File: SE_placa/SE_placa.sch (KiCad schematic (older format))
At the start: 49 parts, among them J1 5V, J2 Micro_SD_Card_Det_Hirose_DM3AT, J3 Conn_02x07_ESP32_IO, J4 I2C-0, J5 I2C-1, J6 Conn_02x03_LORA_IO, J7 U.FL-R-SMT(01), J8 UART, J9 Connector Bateria, Q1 BSS138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

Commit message: Actualizacion PCB
Organizo archivos, agrego nuevos elementos a footprint, actualizo net list y actualizo PCB, agrego modelos 3D disponibles. Listo para iniciar ruteo
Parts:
- J7: symbol U.FL-R-SMT_01_:U.FL-R-SMT(01) -> SE_placa-rescue:U.FL-R-SMT(01)-U.FL-R-SMT_01_
- SW1, SW2: footprint B3U-1000P:SW_B3U-1000P -> Button_Switch_SMD:SW_SPST_CK_RS282G05A3
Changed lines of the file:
@@
 F 0 "SW1" H 2675 7035 50  0000 C CNN
 F 1 "SW_Push_Download" H 2675 6944 50  0000 C CNN
-F 2 "B3U-1000P:SW_B3U-1000P" H 2675 6950 50  0001 C CNN
+F 2 "Button_Switch_SMD:SW_SPST_CK_RS282G05A3" H 2675 6950 50  0001 C CNN
 F 3 "~" H 2675 6950 50  0001 C CNN
 	1    2675 6750
@@
 F 0 "SW2" H 2990 4680 50  0000 C CNN
 F 1 "SW_Push_ESP_RST" H 3255 4595 50  0000 C CNN
-F 2 "B3U-1000P:SW_B3U-1000P" H 3275 4625 50  0001 C CNN
+F 2 "Button_Switch_SMD:SW_SPST_CK_RS282G05A3" H 3275 4625 50  0001 C CNN
 F 3 "~" H 3275 4625 50  0001 C CNN
 	1    3275 4425
@@
 $EndComp
 $Comp
-L U.FL-R-SMT_01_:U.FL-R-SMT(01) J7
+L SE_placa-rescue:U.FL-R-SMT(01)-U.FL-R-SMT_01_ J7
 U 1 1 6198A7A3
 P 14750 2600

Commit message: Organizar integrado rev A
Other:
- note added: "I2C-Segundo sensor\n"
- note added: "Indicador VCC Lora"
- note added: "Indicador VCC general\n"
- note removed: "I2C-spare"
- moved on the sheet: J4, J5, R12, R13
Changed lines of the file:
@@
 Sheet 1 2
 Title "SE_1"
-Date "2021-05-05"
-Rev "1.0"
+Date "2021-07-01"
+Rev "B"
 Comp "Universidad Nacional de Colombia"
 Comment1 "Wilson Poveda"
@@
 L Connector_Generic:Conn_01x04 J4
 U 1 1 60980048
-P 9375 8550
-F 0 "J4" H 9455 8542 50  0000 L CNN
-F 1 "I2C-0" H 9455 8451 50  0000 L CNN
-F 2 "Connector_PinSocket_2.54mm:PinSocket_1x04_P2.54mm_Vertical" H 9375 8550 50  0001 C CNN
-F 3 "~" H 9375 8550 50  0001 C CNN
-	1    9375 8550
+P 9625 8775
+F 0 "J4" H 9705 8767 50  0000 L CNN
+F 1 "I2C-0" H 9705 8676 50  0000 L CNN
+F 2 "Connector_PinSocket_2.54mm:PinSocket_1x04_P2.54mm_Vertical" H 9625 8775 50  0001 C CNN
+F 3 "~" H 9625 8775 50  0001 C CNN
+	1    9625 8775
 	1    0    0    -1
 $EndComp
@@
 Text Label 11100 3000 0    50   ~ 0
 I2C-SDA
-Text Label 8600 8450 0    50   ~ 0
+Text Label 8850 8675 0    50   ~ 0
 I2C-SDA
-Text Label 8600 8550 0    50   ~ 0
+Text Label 8850 8775 0    50   ~ 0
 I2C-SCL
 Text Notes 750  910  0    157  ~ 31
 POWER
-Text Notes 8550 9450 0    118  ~ 0
+Text Notes 8250 8300 0    118  ~ 0
 I2C- BMP180 - BY-68
 Text Notes 715  8240 0    157  ~ 31
@@
 L power:GND #PWR018
 U 1 1 6177D577
-P 8225 8750
-F 0 "#PWR018" H 8225 8500 50  0001 C CNN
-F 1 "GND" H 8230 8577 50  0000 C CNN
-F 2 "" H 8225 8750 50  0001 C CNN
-F 3 "" H 8225 8750 50  0001 C CNN
-	1    8225 8750
+P 8475 8975
+F 0 "#PWR018" H 8475 8725 50  0001 C CNN
+F 1 "GND" H 8480 8802 50  0000 C CNN
+F 2 "" H 8475 8975 50  0001 C CNN
+F 3 "" H 8475 8975 50  0001 C CNN
+	1    8475 8975
 	1    0    0    -1
 $EndComp
@@
 Text Notes 7380 8310 0    157  ~ 31
 I2C\n
-Text Notes 8750 10950 0    118  ~ 0
-I2C-spare
+Text Notes 8600 9900 0    118  ~ 0
+I2C-Segundo sensor\n
 $Comp
 L Connector_Generic:Conn_02x03_Top_Bottom J6
@@
 L Device:R R13
 U 1 1 60AD4FD0
-P 8025 10500
-F 0 "R13" V 7925 10500 50  0000 C CNN
-F 1 "4.7K(5%)" V 8125 10525 50  0000 C CNN
-F 2 "Resistor_SMD:R_0805_2012Metric_Pad1.20x1.40mm_HandSolder" V 7955 10500 50  0001 C CNN
-F 3 "~" H 8025 10500 50  0001 C CNN
-	1    8025 10500
+P 8075 10775
+F 0 "R13" V 7975 10775 50  0000 C CNN
+F 1 "4.7K(5%)" V 8175 10800 50  0000 C CNN
+F 2 "Resistor_SMD:R_0805_2012Metric_Pad1.20x1.40mm_HandSolder" V 8005 10775 50  0001 C CNN
+F 3 "~" H 8075 10775 50  0001 C CNN
+	1    8075 10775
 	0    1    1    0
 $EndComp
@@
 L Device:R R12
 U 1 1 60AD5CFB
-P 8025 9900
-F 0 "R12" V 7818 9900 50  0000 C CNN
-F 1 "4.7K(5%)" V 7909 9900 50  0000 C CNN
-F 2 "Resistor_SMD:R_0805_2012Metric_Pad1.20x1.40mm_HandSolder" V 7955 9900 50  0001 C CNN
-F 3 "~" H 8025 9900 50  0001 C CNN
-	1    8025 9900
+P 8075 10175
+F 0 "R12" V 7868 10175 50  0000 C CNN
+F 1 "4.7K(5%)" V 7959 10175 50  0000 C CNN
+F 2 "Resistor_SMD:R_0805_2012Metric_Pad1.20x1.40mm_HandSolder" V 8005 10175 50  0001 C CNN
+F 3 "~" H 8075 10175 50  0001 C CNN
+	1    8075 10175
 	0    1    1    0
 $EndComp
 Wire Wire Line
-	7875 10500 7875 10200
-Wire Wire Line
-	7875 10200 7575 10200
-Connection ~ 7875 10200
-Wire Wire Line
-	7875 10200 7875 9900
+	7925 10775 7925 10475
+Wire Wire Line
+	7925 10475 7625 10475
+Connection ~ 7925 10475
+Wire Wire Line
+	7925 10475 7925 10175
 Wire Wire Line
 	9300 2400 9000 2400
@@
 Connection ~ 13950 6550
 Wire Wire Line
-	8600 8450 9175 8450
-Wire Wire Line
-	8600 8550 9175 8550
+	8850 8675 9425 8675
+Wire Wire Line
+	8850 8775 9425 8775
 $Comp
 L power:+3V3 #PWR019
 U 1 1 61EE58C6
-P 8550 8825
-F 0 "#PWR019" H 8550 8675 50  0001 C CNN
-F 1 "+3V3" H 8565 8998 50  0000 C CNN
-F 2 "" H 8550 8825 50  0001 C CNN
-F 3 "" H 8550 8825 50  0001 C CNN
-	1    8550 8825
+P 8800 9050
+F 0 "#PWR019" H 8800 8900 50  0001 C CNN
+F 1 "+3V3" H 8815 9223 50  0000 C CNN
+F 2 "" H 8800 9050 50  0001 C CNN
+F 3 "" H 8800 9050 50  0001 C CNN
+	1    8800 9050
 	-1   0    0    1
 $EndComp
 Wire Wire Line
-	8225 8650 8225 8750
-Wire Wire Line
-	8225 8650 9175 8650
-Wire Wire Line
-	8550 8750 8550 8825
-Wire Wire Line
-	8550 8750 9175 8750
+	8475 8875 8475 8975
+Wire Wire Line
+	8475 8875 9425 8875
+Wire Wire Line
+	8800 8975 8800 9050
+Wire Wire Line
+	8800 8975 9425 8975
 $Comp
 L power:+3V3 #PWR013
 U 1 1 61F0C445
-P 7575 10200
-F 0 "#PWR013" H 7575 10050 50  0001 C CNN
-F 1 "+3V3" H 7590 10373 50  0000 C CNN
-F 2 "" H 7575 10200 50  0001 C CNN
-F 3 "" H 7575 10200 50  0001 C CNN
-	1    7575 10200
-	1    0    0    -1
-$EndComp
-Wire Wire Line
-	8175 9900 8550 9900
-Wire Wire Line
-	8175 10500 8575 10500
-Text Label 8550 9900 0    50   ~ 0
+P 7625 10475
+F 0 "#PWR013" H 7625 10325 50  0001 C CNN
+F 1 "+3V3" H 7640 10648 50  0000 C CNN
+F 2 "" H 7625 10475 50  0001 C CNN
+F 3 "" H 7625 10475 50  0001 C CNN
+	1    7625 10475
+	1    0    0    -1
+$EndComp
+Wire Wire Line
+	8225 10175 8600 10175
+Wire Wire Line
+	8225 10775 8625 10775
+Text Label 8600 10175 0    50   ~ 0
 I2C-SDA
-Text Label 8575 10500 0    50   ~ 0
+Text Label 8625 10775 0    50   ~ 0
 I2C-SCL
 $Comp
 L Connector_Generic:Conn_01x04 J5
 U 1 1 61FC148A
-P 10800 9975
-F 0 "J5" H 10880 9967 50  0000 L CNN
-F 1 "I2C-1" H 10880 9876 50  0000 L CNN
-F 2 "Connector_PinSocket_2.54mm:PinSocket_1x04_P2.54mm_Vertical" H 10800 9975 50  0001 C CNN
-F 3 "~" H 10800 9975 50  0001 C CNN
-	1    10800 9975
-	1    0    0    -1
-$EndComp
-Text Label 10025 9875 0    50   ~ 0
+P 10850 10250
+F 0 "J5" H 10930 10242 50  0000 L CNN
+F 1 "I2C-1" H 10930 10151 50  0000 L CNN
+F 2 "Connector_PinSocket_2.54mm:PinSocket_1x04_P2.54mm_Vertical" H 10850 10250 50  0001 C CNN
+F 3 "~" H 10850 10250 50  0001 C CNN
+	1    10850 10250
+	1    0    0    -1
+$EndComp
+Text Label 10075 10150 0    50   ~ 0
 I2C-SDA
-Text Label 10025 9975 0    50   ~ 0
+Text Label 10075 10250 0    50   ~ 0
 I2C-SCL
 $Comp
 L power:GND #PWR022
 U 1 1 61FC16B4
-P 9650 10175
-F 0 "#PWR022" H 9650 9925 50  0001 C CNN
-F 1 "GND" H 9655 10002 50  0000 C CNN
-F 2 "" H 9650 10175 50  0001 C CNN
-F 3 "" H 9650 10175 50  0001 C CNN
-	1    9650 10175
-	1    0    0    -1
-$EndComp
-Wire Wire Line
-	10025 9875 10600 9875
-Wire Wire Line
-	10025 9975 10600 9975
+P 9700 10450
+F 0 "#PWR022" H 9700 10200 50  0001 C CNN
+F 1 "GND" H 9705 10277 50  0000 C CNN
+F 2 "" H 9700 10450 50  0001 C CNN
+F 3 "" H 9700 10450 50  0001 C CNN
+	1    9700 10450
+	1    0    0    -1
+$EndComp
+Wire Wire Line
+	10075 10150 10650 10150
+Wire Wire Line
+	10075 10250 10650 10250
 $Comp
 L power:+3V3 #PWR023
 U 1 1 61FC16C0
-P 9975 10250
-F 0 "#PWR023" H 9975 10100 50  0001 C CNN
-F 1 "+3V3" H 9990 10423 50  0000 C CNN
-F 2 "" H 9975 10250 50  0001 C CNN
-F 3 "" H 9975 10250 50  0001 C CNN
-	1    9975 10250
+P 10025 10525
+F 0 "#PWR023" H 10025 10375 50  0001 C CNN
+F 1 "+3V3" H 10040 10698 50  0000 C CNN
+F 2 "" H 10025 10525 50  0001 C CNN
+F 3 "" H 10025 10525 50  0001 C CNN
+	1    10025 10525
 	-1   0    0    1
 $EndComp
 Wire Wire Line
-	9650 10075 9650 10175
-Wire Wire Line
-	9650 10075 10600 10075
-Wire Wire Line
-	9975 10175 9975 10250
-Wire Wire Line
-	9975 10175 10600 10175
+	9700 10350 9700 10450
+Wire Wire Line
+	9700 10350 10650 10350
+Wire Wire Line
+	10025 10450 10025 10525
+Wire Wire Line
+	10025 10450 10650 10450
 $Comp
 L power:+3V3 #PWR026
@@
 Wire Wire Line
 	15325 9475 15325 9575
+Text Notes 12125 8900 0    50   ~ 0
+Indicador VCC general\n
+Text Notes 14025 9725 0    50   ~ 0
+Indicador VCC Lora
 $EndSCHEMATC

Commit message: Ubicaciones de librerias de absolutas a relativas
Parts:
- J7: footprint U:HRS_U.FL-R-SMT(01) -> HRS_U.FL-R-SMT(01)
- U1: symbol esp32-wrover:ESP32-WROVER -> SE_placa-rescue:ESP32-WROVER-esp32-wrover
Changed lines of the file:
@@
 F 0 "J7" H 14952 2640 50  0000 L CNN
 F 1 "U.FL-R-SMT(01)" H 14995 2525 50  0000 L CNN
-F 2 "U:HRS_U.FL-R-SMT(01)" H 14750 2600 50  0001 L BNN
+F 2 "HRS_U.FL-R-SMT(01)" H 14750 2600 50  0001 L BNN
 F 3 "https://www.sigmaelectronica.net/producto/con-u-fl-smd-m/" H 14750 2600 50  0001 L BNN
 F 4 "Hirose" H 14750 2600 50  0001 L BNN "MF"
@@
 	9300 3900 8800 3900
 $Comp
-L esp32-wrover:ESP32-WROVER U1
+L SE_placa-rescue:ESP32-WROVER-esp32-wrover U1
 U 1 1 6077AD20
 P 10200 3150
@@
 F 1 "Micro_SD_Card_Det_Hirose_DM3AT" H 5100 10526 50  0000 C CNN
 F 2 "Connector_Card:microSD_HC_Hirose_DM3AT-SF-PEJM5" H 7200 10500 50  0001 C CNN
-F 3 "https://www.sigmaelectronica.net/producto/dm3at/" H 5150 9900 50  0001 C CNN
+F 3 "https://www.hirose.com/product/en/download_file/key_name/DM3/category/Catalog/doc_file_id/49662/?file_category_id=4&item_id=195&is_series=1" H 5150 9900 50  0001 C CNN
 	1    5150 9800
 	1    0    0    -1

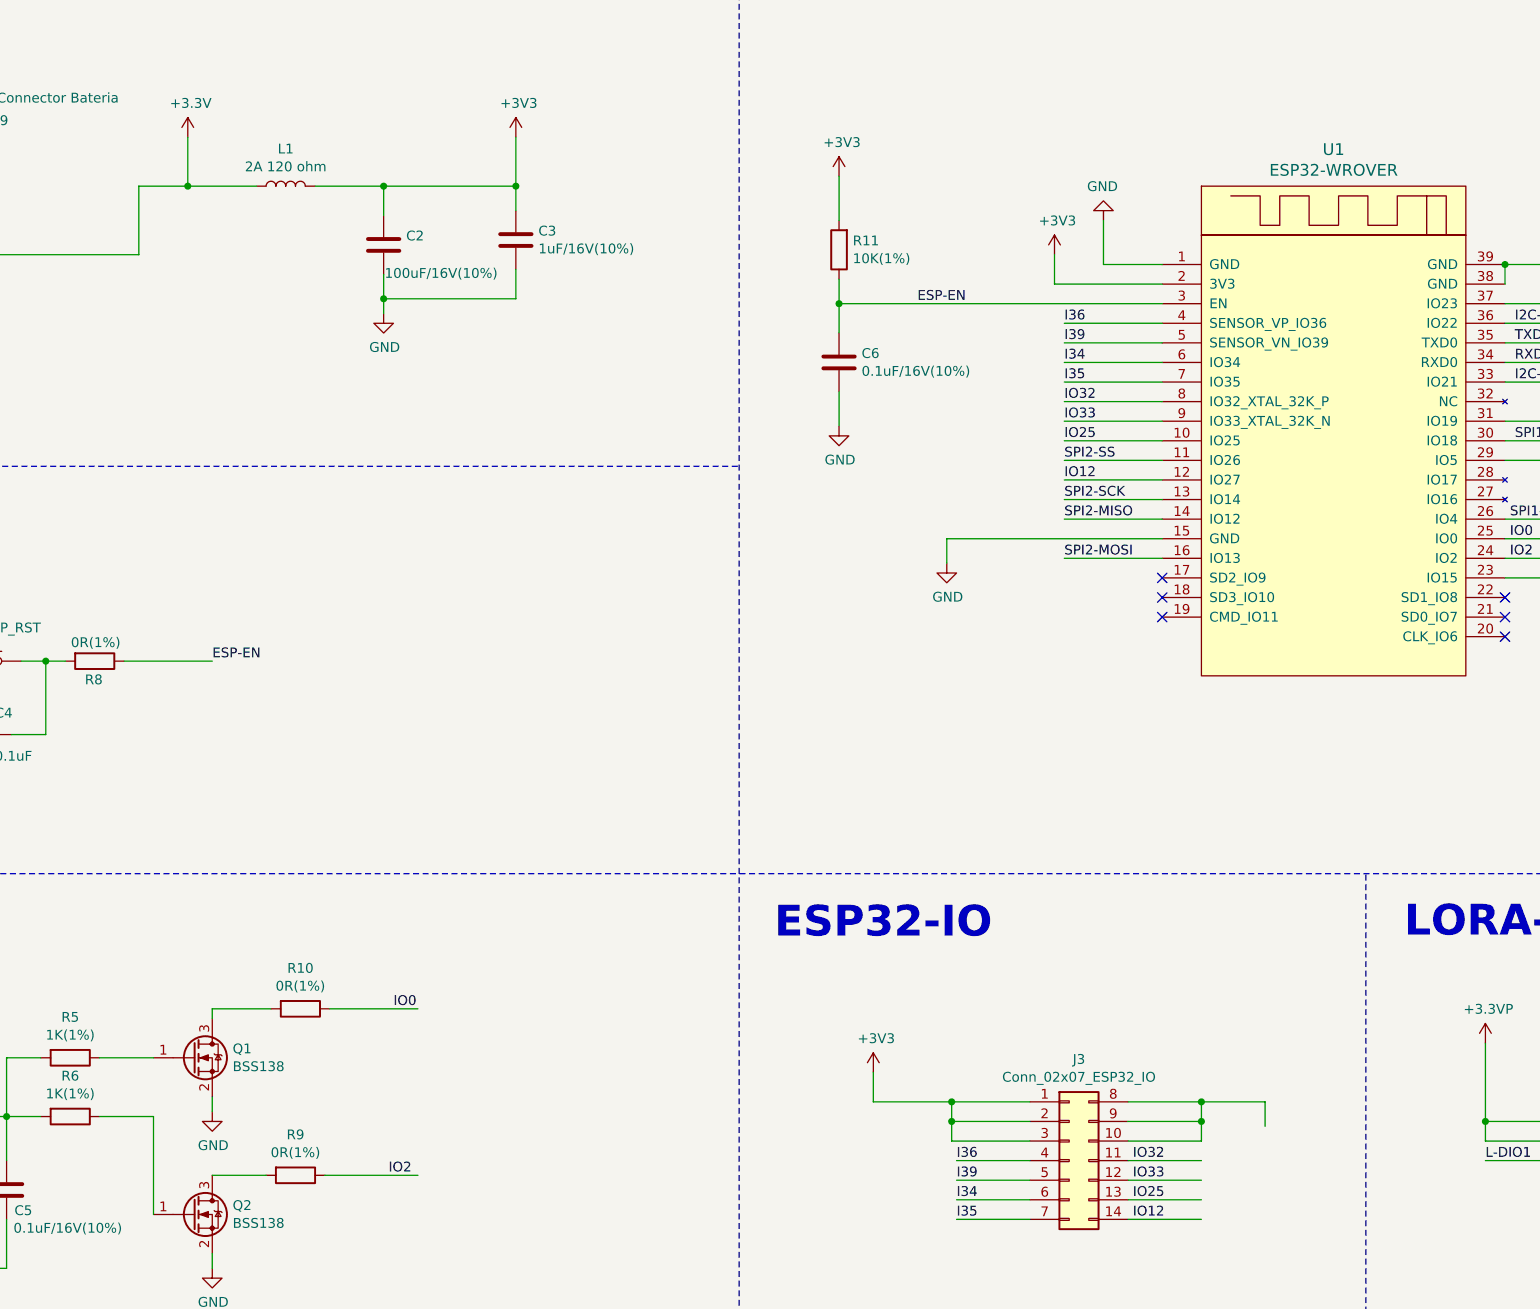
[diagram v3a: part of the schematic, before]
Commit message: ruteo 1
1. Agregados mounting holes 2.5 mm
2. Reordeno elementos para hacer mas facil el ruteo.
3. Ordeno los leds para indicar mejor el estado de lora y alimentacion general
4. Ordeno lesd y conectores de bateria y alimentacion por panel
giro conectores de I/o de lora
en general se dejaron por grupos los elementos de acuerdo al tipo de funcion dentro de la placa
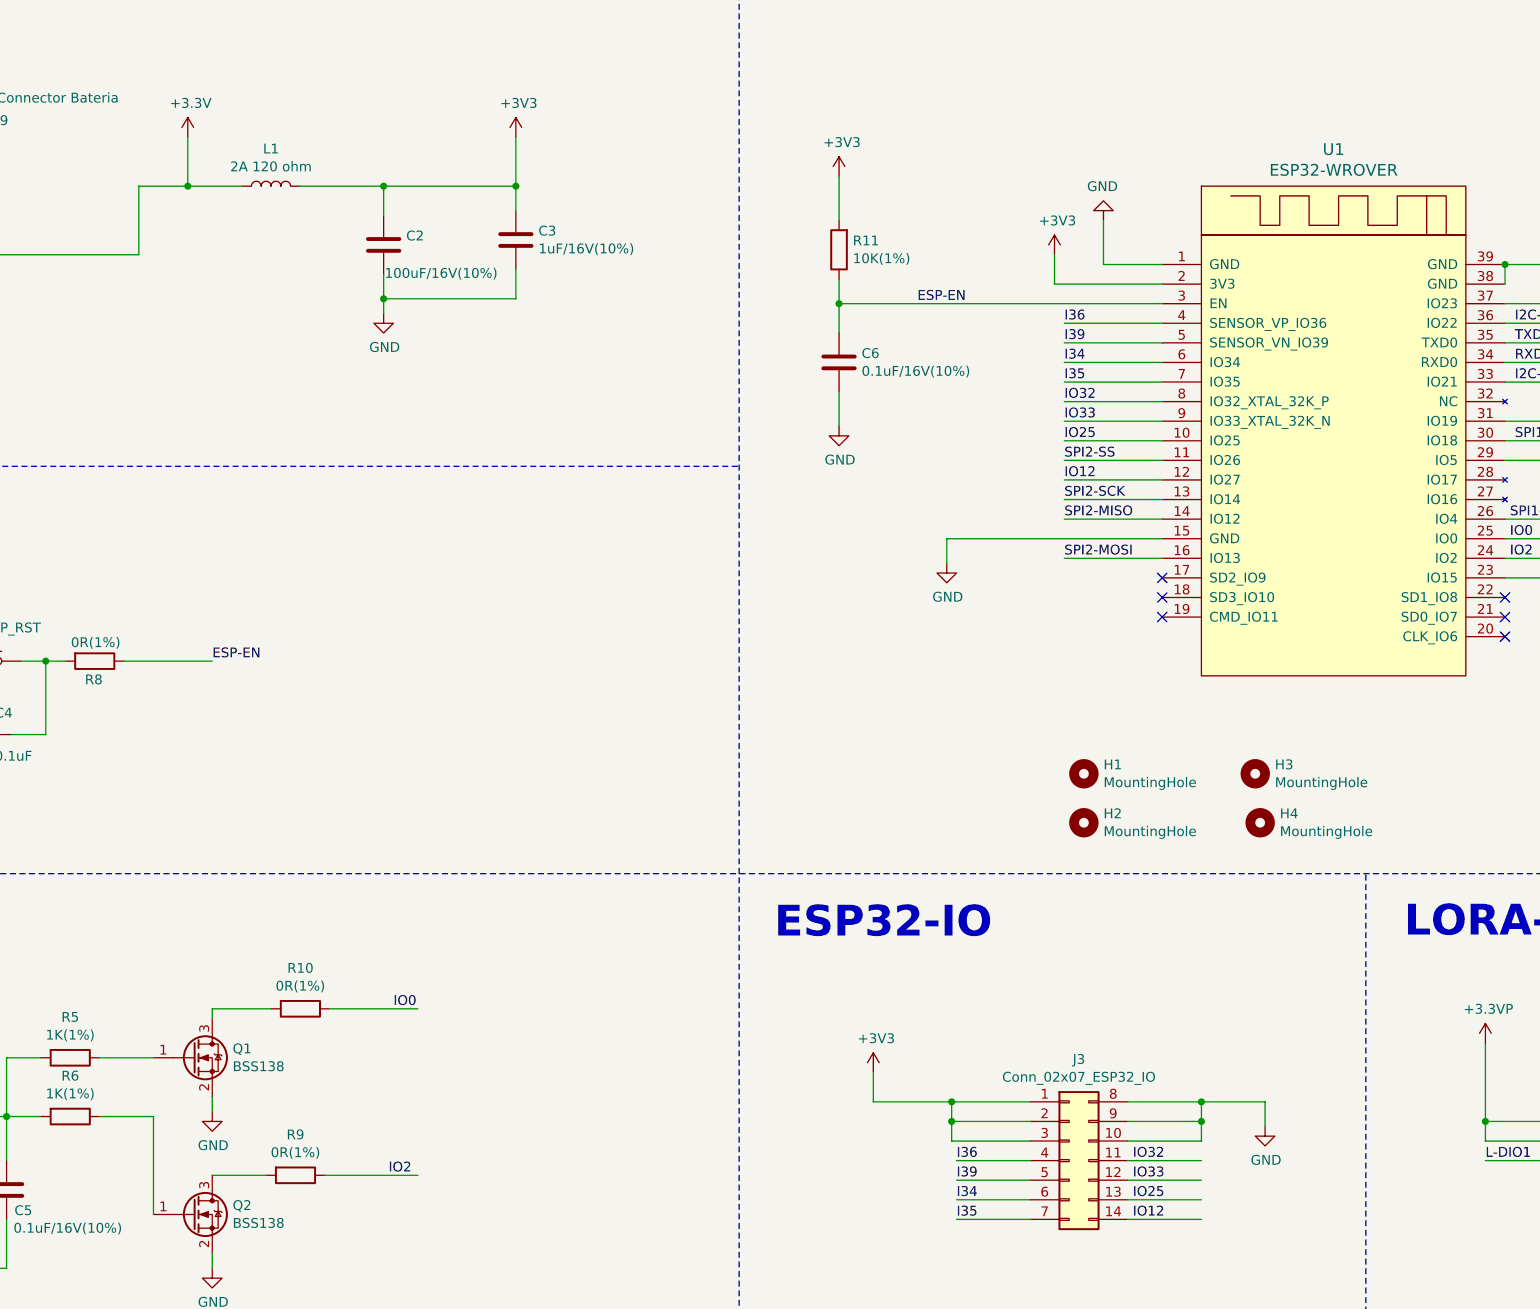
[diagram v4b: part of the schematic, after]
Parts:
- added H1, H2, H3, H4: MountingHole, MountingHole:MountingHole_2.5mm_Pad, symbol Mechanical:MountingHole
- J7: footprint HRS_U.FL-R-SMT(01) -> U:HRS_U.FL-R-SMT(01)
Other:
- moved on the sheet: L1
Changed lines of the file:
@@
 F 0 "J7" H 14952 2640 50  0000 L CNN
 F 1 "U.FL-R-SMT(01)" H 14995 2525 50  0000 L CNN
-F 2 "HRS_U.FL-R-SMT(01)" H 14750 2600 50  0001 L BNN
+F 2 "U:HRS_U.FL-R-SMT(01)" H 14750 2600 50  0001 L BNN
 F 3 "https://www.sigmaelectronica.net/producto/con-u-fl-smd-m/" H 14750 2600 50  0001 L BNN
 F 4 "Hirose" H 14750 2600 50  0001 L BNN "MF"
@@
 	5325 2450 5325 2575
 Wire Wire Line
-	5325 2000 6000 2000
-Wire Wire Line
 	5325 2150 5325 2000
 Wire Wire Line
@@
 Wire Wire Line
 	6000 2000 6000 1750
-Connection ~ 5325 2000
-Wire Wire Line
-	4975 2000 5325 2000
-Wire Wire Line
-	4325 2000 4675 2000
-Wire Wire Line
-	4325 1750 4325 2000
-Connection ~ 4325 2000
 $Comp
 L power:+3V3 #PWR043
@@
 L Device:L L1
 U 1 1 60B718E1
-P 4825 2000
+P 4750 2000
 AR Path="/60B718E1" Ref="L1"  Part="1"
 AR Path="/609FB393/60B718E1" Ref="L?"  Part="1"
-F 0 "L1" V 5015 2000 50  0000 C CNN
-F 1 "2A 120 ohm" V 4924 2000 50  0000 C CNN
-F 2 "Inductor_SMD:L_0805_2012Metric_Pad1.15x1.40mm_HandSolder" H 4825 2000 50  0001 C CNN
-F 3 "~" H 4825 2000 50  0001 C CNN
-	1    4825 2000
+F 0 "L1" V 4940 2000 50  0000 C CNN
+F 1 "2A 120 ohm" V 4849 2000 50  0000 C CNN
+F 2 "Inductor_SMD:L_0805_2012Metric_Pad1.15x1.40mm_HandSolder" H 4750 2000 50  0001 C CNN
+F 3 "~" H 4750 2000 50  0001 C CNN
+	1    4750 2000
 	0    -1   -1   0
 $EndComp
@@
 Wire Wire Line
 	4075 2350 4075 2000
-Wire Wire Line
-	4075 2000 4325 2000
 $Comp
 L power:GND #PWR0101
@@
 Text Notes 14025 9725 0    50   ~ 0
 Indicador VCC Lora
+$Comp
+L Mechanical:MountingHole H2
+U 1 1 60EF16A7
+P 8900 5250
+F 0 "H2" H 9000 5296 50  0000 L CNN
+F 1 "MountingHole" H 9000 5205 50  0000 L CNN
+F 2 "MountingHole:MountingHole_2.5mm_Pad" H 8900 5250 50  0001 C CNN
+F 3 "~" H 8900 5250 50  0001 C CNN
+	1    8900 5250
+	1    0    0    -1
+$EndComp
+$Comp
+L Mechanical:MountingHole H4
+U 1 1 60EF1BF8
+P 9800 5250
+F 0 "H4" H 9900 5296 50  0000 L CNN
+F 1 "MountingHole" H 9900 5205 50  0000 L CNN
+F 2 "MountingHole:MountingHole_2.5mm_Pad" H 9800 5250 50  0001 C CNN
+F 3 "~" H 9800 5250 50  0001 C CNN
+	1    9800 5250
+	1    0    0    -1
+$EndComp
+$Comp
+L Mechanical:MountingHole H3
+U 1 1 60EF20E2
+P 9775 5000
+F 0 "H3" H 9875 5046 50  0000 L CNN
+F 1 "MountingHole" H 9875 4955 50  0000 L CNN
+F 2 "MountingHole:MountingHole_2.5mm_Pad" H 9775 5000 50  0001 C CNN
+F 3 "~" H 9775 5000 50  0001 C CNN
+	1    9775 5000
+	1    0    0    -1
+$EndComp
+$Comp
+L Mechanical:MountingHole H1
+U 1 1 60EF23F0
+P 8900 5000
+F 0 "H1" H 9000 5046 50  0000 L CNN
+F 1 "MountingHole" H 9000 4955 50  0000 L CNN
+F 2 "MountingHole:MountingHole_2.5mm_Pad" H 8900 5000 50  0001 C CNN
+F 3 "~" H 8900 5000 50  0001 C CNN
+	1    8900 5000
+	1    0    0    -1
+$EndComp
+$Comp
+L power:GND #PWR0102
+U 1 1 60FEDC40
+P 9825 6800
+F 0 "#PWR0102" H 9825 6550 50  0001 C CNN
+F 1 "GND" H 9830 6627 50  0000 C CNN
+F 2 "" H 9825 6800 50  0001 C CNN
+F 3 "" H 9825 6800 50  0001 C CNN
+	1    9825 6800
+	1    0    0    -1
+$EndComp
+Wire Wire Line
+	5325 2000 6000 2000
+Wire Wire Line
+	5325 2000 4900 2000
+Connection ~ 5325 2000
+Wire Wire Line
+	4600 2000 4325 2000
+Wire Wire Line
+	4325 1750 4325 2000
+Connection ~ 4325 2000
+Wire Wire Line
+	4325 2000 4075 2000
 $EndSCHEMATC
